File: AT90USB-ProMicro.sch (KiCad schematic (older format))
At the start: 15 parts, among them J1 Conn_01x12, J2 Conn_01x12, U1 AT90USB162-16MU, U2 MCP1703A-3302_SOT23, X1 ECS-2520MV-xxx-xx

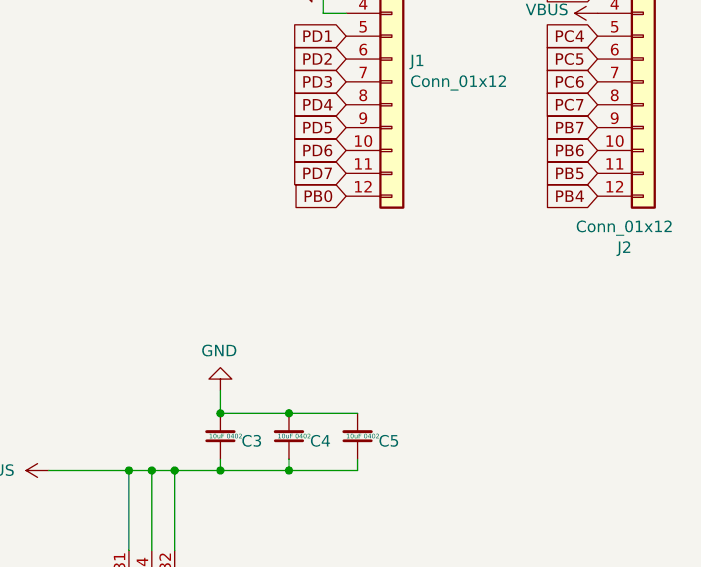
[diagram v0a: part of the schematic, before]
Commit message: broke out spare MCU pins to a header.
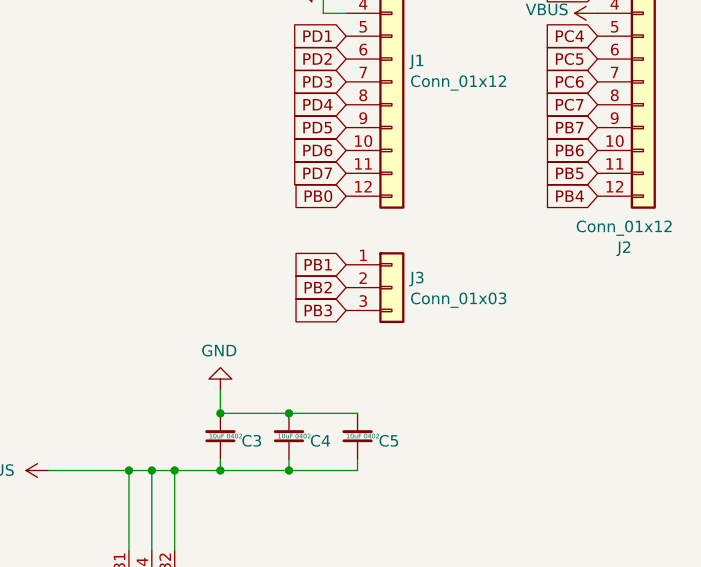
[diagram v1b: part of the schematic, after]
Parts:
- added J3: Conn_01x03, Connector_PinHeader_2.54mm:PinHeader_1x03_P2.54mm_Vertical, symbol Connector_Generic:Conn_01x03
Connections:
- net PB1: now also J3.1 (Pin_1)
- net PB2: now also J3.2 (Pin_2)
- net PB3: now also J3.3 (Pin_3)
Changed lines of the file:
@@
 Text GLabel 6350 2550 0    50   Input ~ 0
 PB0
+Text GLabel 6350 2850 0    50   Input ~ 0
+PB1
+Text GLabel 6350 2950 0    50   Input ~ 0
+PB2
+Text GLabel 6350 3050 0    50   Input ~ 0
+PB3
+$Comp
+L Connector_Generic:Conn_01x03 J3
+U 1 1 610C3681
+P 6550 2950
+F 0 "J3" H 6630 2992 50  0000 L CNN
+F 1 "Conn_01x03" H 6630 2901 50  0000 L CNN
+F 2 "Connector_PinHeader_2.54mm:PinHeader_1x03_P2.54mm_Vertical" H 6550 2950 50  0001 C CNN
+F 3 "~" H 6550 2950 50  0001 C CNN
+	1    6550 2950
+	1    0    0    -1
+$EndComp
 $EndSCHEMATC

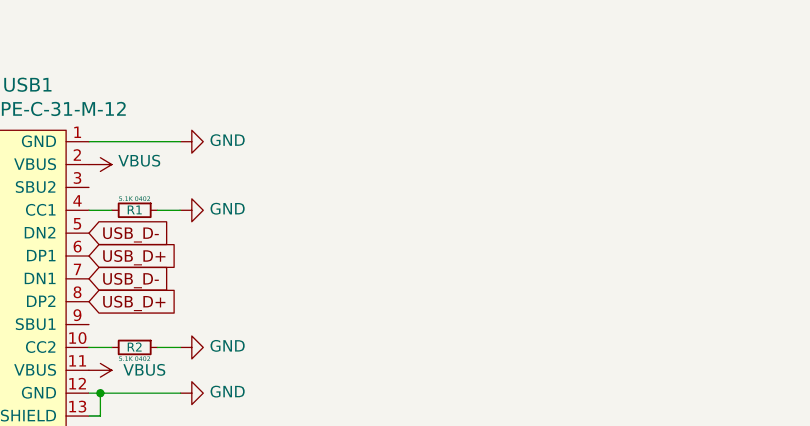
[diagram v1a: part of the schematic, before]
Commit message: Added some silkscreen notes and realigned some capacitors, resistors and usb traces
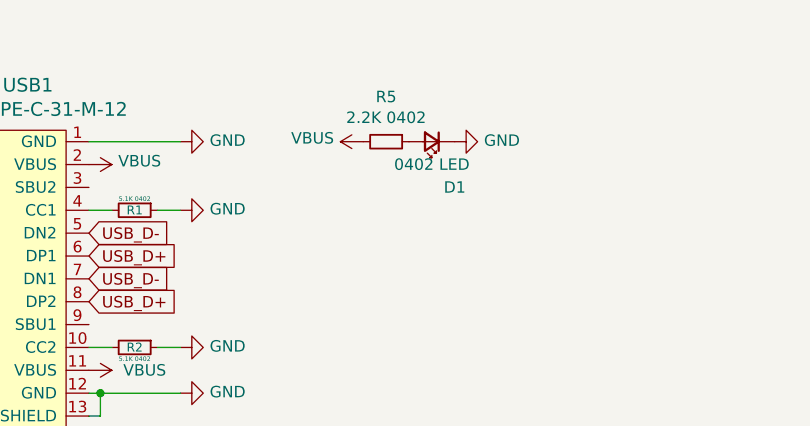
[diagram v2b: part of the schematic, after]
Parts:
- added D1: 0402 LED, LED_SMD:LED_0402_1005Metric, symbol Device:LED_Small
- added R5: 2.2K 0402, Resistor_SMD:R_0402_1005Metric, symbol Device:R_Small
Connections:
- net GND: now also D1.1 (K)
- net VBUS: now also R5.2
- new net: D1.2 (A), R5.1
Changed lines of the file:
@@
 	1    0    0    -1
 $EndComp
+$Comp
+L power:VBUS #PWR0118
+U 1 1 610C1571
+P 2850 1900
+F 0 "#PWR0118" H 2850 1750 50  0001 C CNN
+F 1 "VBUS" V 2865 2028 50  0000 L CNN
+F 2 "" H 2850 1900 50  0001 C CNN
+F 3 "" H 2850 1900 50  0001 C CNN
+	1    2850 1900
+	0    -1   -1   0
+$EndComp
+$Comp
+L Device:LED_Small D1
+U 1 1 610C23BA
+P 3150 1900
+F 0 "D1" H 3050 2100 50  0000 C CNN
+F 1 "0402 LED" H 3150 2000 50  0000 C CNN
+F 2 "LED_SMD:LED_0402_1005Metric" V 3150 1900 50  0001 C CNN
+F 3 "~" V 3150 1900 50  0001 C CNN
+	1    3150 1900
+	-1   0    0    1
+$EndComp
+$Comp
+L power:GND #PWR0119
+U 1 1 610C2E7E
+P 3250 1900
+F 0 "#PWR0119" H 3250 1650 50  0001 C CNN
+F 1 "GND" V 3255 1772 50  0000 R CNN
+F 2 "" H 3250 1900 50  0001 C CNN
+F 3 "" H 3250 1900 50  0001 C CNN
+	1    3250 1900
+	0    -1   -1   0
+$EndComp
+$Comp
+L Device:R_Small R5
+U 1 1 610C7415
+P 2950 1900
+F 0 "R5" V 2754 1900 50  0000 C CNN
+F 1 "2.2K 0402" V 2845 1900 50  0000 C CNN
+F 2 "Resistor_SMD:R_0402_1005Metric" H 2950 1900 50  0001 C CNN
+F 3 "~" H 2950 1900 50  0001 C CNN
+	1    2950 1900
+	0    1    1    0
+$EndComp
 $EndSCHEMATC

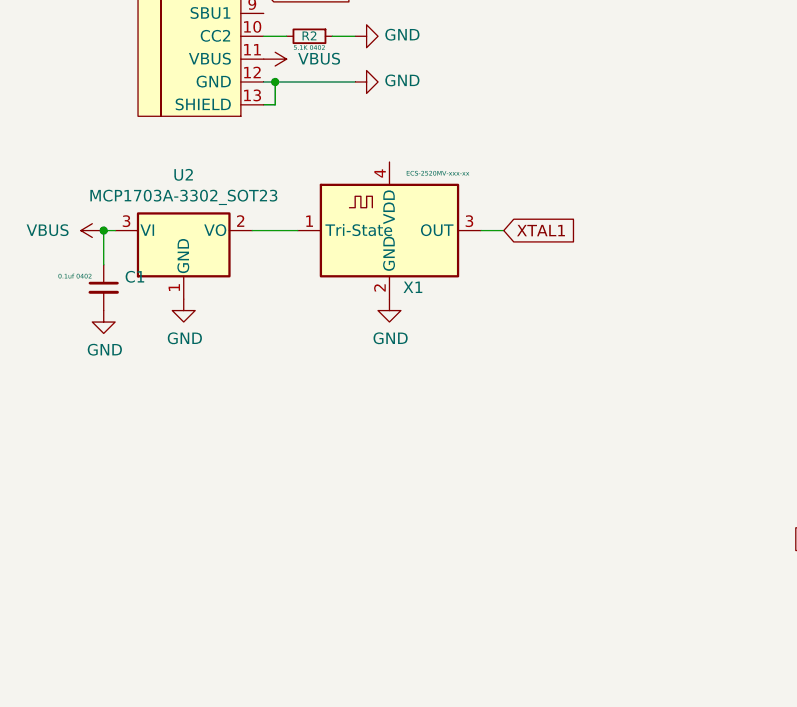
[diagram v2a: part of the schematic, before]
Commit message: added a couple more decoupling capacitors, one for 3.3V LDO and one for the clock
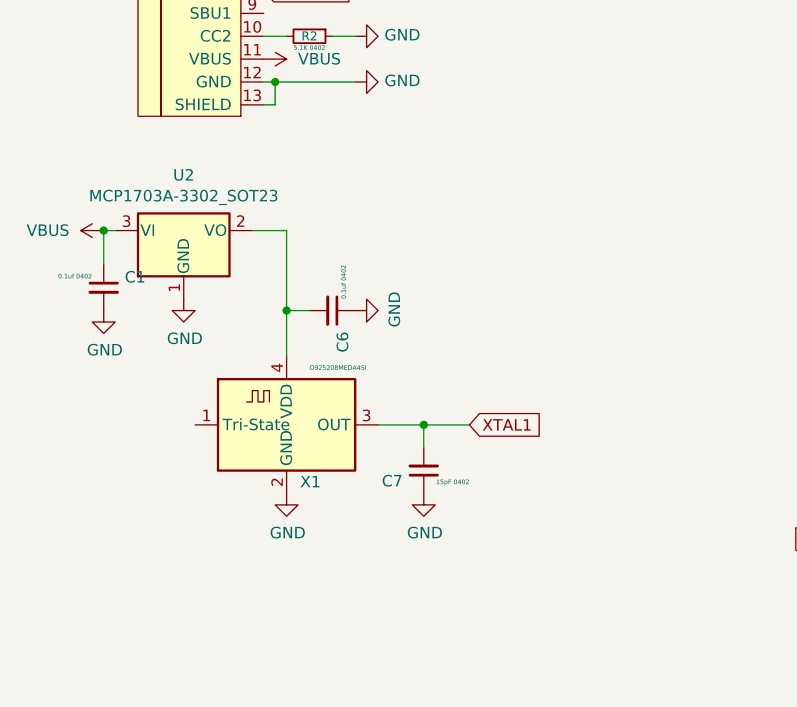
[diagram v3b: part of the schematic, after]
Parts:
- added C6: 0.1uf 0402, Capacitor_SMD:C_0402_1005Metric, symbol Device:C_Small
- added C7: 15pF 0402, Capacitor_SMD:C_0402_1005Metric, symbol Device:C_Small
- X1: value ECS-2520MV-xxx-xx -> O925208MEDA4SI
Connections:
- net GND: now also C6.1, C7.1
- net XTAL1: now also C7.2
- net at U2.2 (VO): now also X1.4 (VDD), C6.2; no longer X1.1 (Tri-State)
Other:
- moved on the sheet: X1
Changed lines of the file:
@@
 Text GLabel 4800 4600 0    50   Input ~ 0
 XTAL1
-Text GLabel 2700 3650 2    50   Input ~ 0
+Text GLabel 2550 4500 2    50   Input ~ 0
 XTAL1
 $Comp
@@
 L Oscillator:ECS-2520MV-xxx-xx X1
 U 1 1 611038B7
-P 2200 3650
-F 0 "X1" H 2350 3400 50  0000 R CNN
-F 1 "ECS-2520MV-xxx-xx" H 2550 3900 20  0000 R CNN
-F 2 "Oscillator:Oscillator_SMD_ECS_2520MV-xxx-xx-4Pin_2.5x2.0mm" H 2650 3300 50  0001 C CNN
-F 3 "https://www.ecsxtal.com/store/pdf/ECS-2520MV.pdf" H 2025 3775 50  0001 C CNN
-	1    2200 3650
-	1    0    0    -1
-$EndComp
-Wire Wire Line
-	2700 3650 2600 3650
+P 1750 4500
+F 0 "X1" H 1900 4250 50  0000 R CNN
+F 1 "O925208MEDA4SI" H 2100 4750 20  0000 R CNN
+F 2 "Oscillator:Oscillator_SMD_ECS_2520MV-xxx-xx-4Pin_2.5x2.0mm" H 2200 4150 50  0001 C CNN
+F 3 "https://www.ecsxtal.com/store/pdf/ECS-2520MV.pdf" H 1575 4625 50  0001 C CNN
+	1    1750 4500
+	1    0    0    -1
+$EndComp
 Wire Wire Line
 	950  3650 1000 3650
@@
 L power:GND #PWR0111
 U 1 1 610BE5C3
-P 2200 3950
-F 0 "#PWR0111" H 2200 3700 50  0001 C CNN
-F 1 "GND" H 2205 3777 50  0000 C CNN
-F 2 "" H 2200 3950 50  0001 C CNN
-F 3 "" H 2200 3950 50  0001 C CNN
-	1    2200 3950
+P 1750 4800
+F 0 "#PWR0111" H 1750 4550 50  0001 C CNN
+F 1 "GND" H 1755 4627 50  0000 C CNN
+F 2 "" H 1750 4800 50  0001 C CNN
+F 3 "" H 1750 4800 50  0001 C CNN
+	1    1750 4800
 	1    0    0    -1
 $EndComp
@@
 	1    0    0    -1
 $EndComp
-Wire Wire Line
-	1800 3650 1600 3650
 $Comp
 L power:GND #PWR0113
@@
 	0    1    1    0
 $EndComp
+Wire Wire Line
+	1750 4200 1750 4000
+Wire Wire Line
+	1750 3650 1600 3650
+$Comp
+L Device:C_Small C6
+U 1 1 610DB8B7
+P 1950 4000
+F 0 "C6" H 2042 4046 50  0000 L CNN
+F 1 "0.1uf 0402" H 1750 4050 20  0000 L CNN
+F 2 "Capacitor_SMD:C_0402_1005Metric" H 1950 4000 50  0001 C CNN
+F 3 "~" H 1950 4000 50  0001 C CNN
+	1    1950 4000
+	0    1    1    0
+$EndComp
+$Comp
+L power:GND #PWR02
+U 1 1 610DC063
+P 2050 4000
+F 0 "#PWR02" H 2050 3750 50  0001 C CNN
+F 1 "GND" H 2055 3827 50  0000 C CNN
+F 2 "" H 2050 4000 50  0001 C CNN
+F 3 "" H 2050 4000 50  0001 C CNN
+	1    2050 4000
+	0    -1   -1   0
+$EndComp
+Wire Wire Line
+	1850 4000 1750 4000
+Connection ~ 1750 4000
+Wire Wire Line
+	1750 4000 1750 3650
+$Comp
+L Device:C_Small C7
+U 1 1 610DF85F
+P 2350 4700
+F 0 "C7" H 2442 4746 50  0000 L CNN
+F 1 "15pF 0402" H 2150 4750 20  0000 L CNN
+F 2 "Capacitor_SMD:C_0402_1005Metric" H 2350 4700 50  0001 C CNN
+F 3 "~" H 2350 4700 50  0001 C CNN
+	1    2350 4700
+	-1   0    0    1
+$EndComp
+$Comp
+L power:GND #PWR03
+U 1 1 610DFF21
+P 2350 4800
+F 0 "#PWR03" H 2350 4550 50  0001 C CNN
+F 1 "GND" H 2355 4627 50  0000 C CNN
+F 2 "" H 2350 4800 50  0001 C CNN
+F 3 "" H 2350 4800 50  0001 C CNN
+	1    2350 4800
+	1    0    0    -1
+$EndComp
+Wire Wire Line
+	2150 4500 2350 4500
+Connection ~ 2350 4500
+Wire Wire Line
+	2350 4500 2550 4500
+Wire Wire Line
+	2350 4500 2350 4600
 $EndSCHEMATC

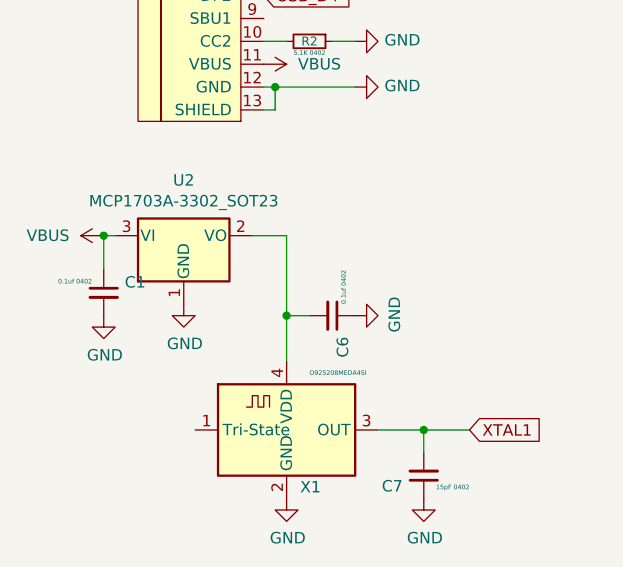
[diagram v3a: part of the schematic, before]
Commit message: changed part description in schematic
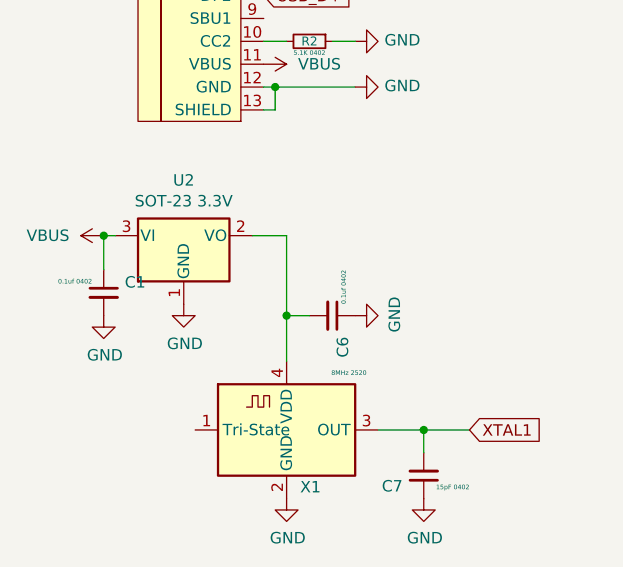
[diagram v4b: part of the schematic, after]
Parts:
- U2: value MCP1703A-3302_SOT23 -> SOT-23 3.3V
- X1: value O925208MEDA4SI -> 8MHz 2520
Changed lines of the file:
@@
 P 1750 4500
 F 0 "X1" H 1900 4250 50  0000 R CNN
-F 1 "O925208MEDA4SI" H 2100 4750 20  0000 R CNN
+F 1 "8MHz 2520" H 2100 4750 20  0000 R CNN
 F 2 "Oscillator:Oscillator_SMD_ECS_2520MV-xxx-xx-4Pin_2.5x2.0mm" H 2200 4150 50  0001 C CNN
 F 3 "https://www.ecsxtal.com/store/pdf/ECS-2520MV.pdf" H 1575 4625 50  0001 C CNN
@@
 P 1300 3650
 F 0 "U2" H 1300 3892 50  0000 C CNN
-F 1 "MCP1703A-3302_SOT23" H 1300 3801 50  0000 C CNN
+F 1 "SOT-23 3.3V" H 1300 3801 50  0000 C CNN
 F 2 "Package_TO_SOT_SMD:SOT-23" H 1300 3850 50  0001 C CNN
 F 3 "http://ww1.microchip.com/downloads/en/DeviceDoc/20005122B.pdf" H 1300 3600 50  0001 C CNN
